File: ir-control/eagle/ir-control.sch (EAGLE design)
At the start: 31 parts, among them J1 MICRO USB, J2 MICRO USB, J3 MICRO USB, Q1 DTA114EET1G (2x10K), Q3 NPN, U2 NUF2042XV6T1G, U3 LPC11U35FHI33/501, U4 MCP1754ST-3302E/CB, X1 KLBR1, Y1 12Mhz

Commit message: Some cleanups.
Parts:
- removed C17: 0.1uF, ir-control:CC0402K
- removed R13: 1K5, ir-control:RR0402
- removed U4: MCP1754ST-3302E/CB, ir-control:LDO
- removed X1: KLBR1, ir-control:KLBR1
- added C9: 0.1uF, ir-control:CC0402K
- added J4: JACKX, ir-control:JACKX
- added R8: 10K, ir-control:RR0402
- added U1: NUF2042XV6T1G, ir-control:USB-ESD
- C1: value 18pF -> 10u; device ir-control:CC0402K -> ir-control:CC0805K
- C2: value 18pF -> 1u; device ir-control:CC0402K -> ir-control:CC0603K
- C3: value 0.1uF -> 1u; device ir-control:CC0402K -> ir-control:CC0603K
- C4: value 0.1uF -> 10u; device ir-control:CC0402K -> ir-control:CC0805K
- C5: value 10u -> 18pF; device ir-control:CC0805K -> ir-control:CC0402K
- C6: value 1u -> 18pF; device ir-control:CC0603K -> ir-control:CC0402K
- C7: value 1u -> 0.1uF; device ir-control:CC0603K -> ir-control:CC0402K
- C8: value 10u -> 0.1uF; device ir-control:CC0805K -> ir-control:CC0402K
- R1: value 1K5 -> 10K
- R3: value 10K -> 1K5
- R5, R7: value 10K -> 330
- R6: value 330 -> 1K5
- U2: value NUF2042XV6T1G -> MCP1754ST-3302E/CB; device ir-control:USB-ESD -> ir-control:LDO
- renumbered D3 to D1, Y1 to Q2
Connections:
- net !ISP_EN: now also C9.2; no longer C17.2
- net !RESET: now also R8.1; no longer R3.1
- net +3V3: now also C7.1, C8.1, C9.1, R8.2; no longer C17.1, C3.1, C4.1, R3.2
- net +5V: now also C1.1, C2.1, J3.VBUS, R4.1, R7.2, U1.VBUS, U2.VIN; no longer C5.1, C6.1, J1.VBUS, R2.1, R6.2, U2.VBUS, U4.VIN
- net AV_SENSE: now also R2.2, U3.TD/AD0/CT32B0_MAT3/PIO0_11; no longer R5.2
- net GND: now also U1.GND; no longer U4.GND
- net IR: now also R6.2; no longer R7.2
- net LED: now also R5.1; no longer R13.1
- net N$1: now also C5.1; no longer C1.1
- net N$12: now also J3.D-, U1.DMI; no longer J1.D-, U2.DMI
- net N$14: now also R5.2; no longer R13.2
- net N$2: now also J1.VBUS, R1.1; no longer J2.VBUS, R4.1
- net N$3: now also C6.1; no longer C2.1
- net N$4: now also R6.1; no longer R7.1
- net N$5: now also R3.2; no longer R1.2
- net N$6: now also J3.D+, R3.1, U1.DPI; no longer J1.D+, R1.1, U2.DPI
- net N$7: now also J2.VBUS, R2.1; no longer J3.VBUS, R5.1
- net TV_SENSE: now also R1.2, U3.SWCLK/SCK0/CT16B0_MAT2/PIO0_10; no longer R4.2
- net USB_DM: now also U1.DMO; no longer U2.DMO
- net USB_DP: now also U1.DPO; no longer U2.DPO
- net VBUS: now also R4.2; no longer R2.2
- net VOUT: now also C3.1, C4.1, U2.VOUT; no longer C7.1, C8.1, U4.VOUT
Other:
- moved on the sheet: C1, C2, C3, C4, C5, C6, C7, C8, J1, J2, J3, R1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

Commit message: More progress with the layout.
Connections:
- removed net VOUT: C3.1, C4.1, U2.VOUT
- net +3V3: now also C3.1, C4.1, U2.VOUT
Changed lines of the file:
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@@
 <attribute name="VALUE" x="345.186" y="262.382" size="1.778" layer="96"/>
 </instance>
-<instance part="+3V35" gate="G$1" x="342.9" y="271.78"/>
+<instance part="+3V35" gate="G$1" x="342.9" y="274.32"/>
 <instance part="S2" gate="G$1" x="383.54" y="83.82" smashed="yes">
 <attribute name="NAME" x="377.952" y="79.248" size="1.778" layer="95"/>
@@
 <pinref part="R8" gate="G$1" pin="2"/>
 <pinref part="+3V35" gate="G$1" pin="+3V3"/>
+<wire x1="342.9" y1="271.78" x2="342.9" y2="269.24" width="0.1524" layer="91"/>
 </segment>
 <segment>
@@
 <wire x1="350.52" y1="109.22" x2="350.52" y2="111.76" width="0.1524" layer="91"/>
 <pinref part="+3V36" gate="G$1" pin="+3V3"/>
+</segment>
+<segment>
+<pinref part="C3" gate="G$1" pin="1"/>
+<wire x1="210.82" y1="119.38" x2="220.98" y2="119.38" width="0.1524" layer="91"/>
+<wire x1="220.98" y1="119.38" x2="226.06" y2="119.38" width="0.1524" layer="91"/>
+<wire x1="210.82" y1="114.3" x2="210.82" y2="119.38" width="0.1524" layer="91"/>
+<pinref part="+3V32" gate="G$1" pin="+3V3"/>
+<wire x1="220.98" y1="114.3" x2="220.98" y2="119.38" width="0.1524" layer="91"/>
+<junction x="220.98" y="119.38"/>
+<pinref part="C4" gate="G$1" pin="1"/>
+<pinref part="U2" gate="G$1" pin="VOUT"/>
+<wire x1="205.74" y1="119.38" x2="210.82" y2="119.38" width="0.1524" layer="91"/>
+<junction x="210.82" y="119.38"/>
 </segment>
 </net>
@@
 </segment>
 </net>
-<net name="VOUT" class="0">
-<segment>
-<pinref part="C3" gate="G$1" pin="1"/>
-<wire x1="210.82" y1="119.38" x2="220.98" y2="119.38" width="0.1524" layer="91"/>
-<wire x1="220.98" y1="119.38" x2="226.06" y2="119.38" width="0.1524" layer="91"/>
-<wire x1="210.82" y1="114.3" x2="210.82" y2="119.38" width="0.1524" layer="91"/>
-<pinref part="+3V32" gate="G$1" pin="+3V3"/>
-<wire x1="220.98" y1="114.3" x2="220.98" y2="119.38" width="0.1524" layer="91"/>
-<junction x="220.98" y="119.38"/>
-<pinref part="C4" gate="G$1" pin="1"/>
-<pinref part="U2" gate="G$1" pin="VOUT"/>
-<wire x1="205.74" y1="119.38" x2="210.82" y2="119.38" width="0.1524" layer="91"/>
-<junction x="210.82" y="119.38"/>
-</segment>
-</net>

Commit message: More layout cleanup. Still incomplete.
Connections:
- net N$2: now also J2.VBUS; no longer J1.VBUS
- net N$7: now also J1.VBUS; no longer J2.VBUS
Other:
- moved on the sheet: J1, J2
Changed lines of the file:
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@@
 <classes>
 <class number="0" name="default" width="0" drill="0">
+<clearance class="0" value="0.205"/>
 </class>
 <class number="1" name="power" width="0.254" drill="0">
 </class>
 <class number="2" name="critical" width="0" drill="0">
+<clearance class="0" value="0.205"/>
+<clearance class="1" value="0.205"/>
+<clearance class="2" value="0.205"/>
 </class>
 </classes>
@@
 <part name="C4" library="ir-control" deviceset="C" device="C0805K" value="10u"/>
 <part name="U2" library="ir-control" deviceset="LDO" device="" value="MCP1754ST-3302E/CB"/>
+<part name="J2" library="ir-control" deviceset="USB-CONN" device="" value="MICRO USB"/>
 <part name="J1" library="ir-control" deviceset="USB-CONN" device="" value="MICRO USB"/>
-<part name="J2" library="ir-control" deviceset="USB-CONN" device="" value="MICRO USB"/>
 <part name="GND1" library="ir-control" deviceset="GND" device=""/>
 <part name="GND2" library="ir-control" deviceset="GND" device=""/>
@@
 <attribute name="VALUE" x="182.88" y="124.46" size="1.778" layer="96"/>
 </instance>
-<instance part="J1" gate="G$1" x="40.64" y="137.16"/>
-<instance part="J2" gate="G$1" x="40.64" y="73.66"/>
+<instance part="J2" gate="G$1" x="40.64" y="137.16"/>
+<instance part="J1" gate="G$1" x="40.64" y="73.66"/>
 <instance part="GND1" gate="1" x="50.8" y="127"/>
 <instance part="GND2" gate="1" x="50.8" y="63.5"/>
@@
 </segment>
 <segment>
-<pinref part="J2" gate="G$1" pin="GND"/>
+<pinref part="J1" gate="G$1" pin="GND"/>
 <pinref part="GND2" gate="1" pin="GND"/>
 <wire x1="48.26" y1="68.58" x2="50.8" y2="68.58" width="0.1524" layer="91"/>
@@
 </segment>
 <segment>
-<pinref part="J1" gate="G$1" pin="GND"/>
+<pinref part="J2" gate="G$1" pin="GND"/>
 <pinref part="GND1" gate="1" pin="GND"/>
 <wire x1="48.26" y1="132.08" x2="50.8" y2="132.08" width="0.1524" layer="91"/>
@@
 <net name="N$2" class="0">
 <segment>
-<pinref part="J1" gate="G$1" pin="VBUS"/>
+<pinref part="J2" gate="G$1" pin="VBUS"/>
 <pinref part="R1" gate="G$1" pin="1"/>
 <wire x1="48.26" y1="152.4" x2="55.88" y2="152.4" width="0.1524" layer="91"/>
@@
 <net name="N$7" class="0">
 <segment>
-<pinref part="J2" gate="G$1" pin="VBUS"/>
+<pinref part="J1" gate="G$1" pin="VBUS"/>
 <pinref part="R2" gate="G$1" pin="1"/>
 <wire x1="48.26" y1="88.9" x2="55.88" y2="88.9" width="0.1524" layer="91"/>

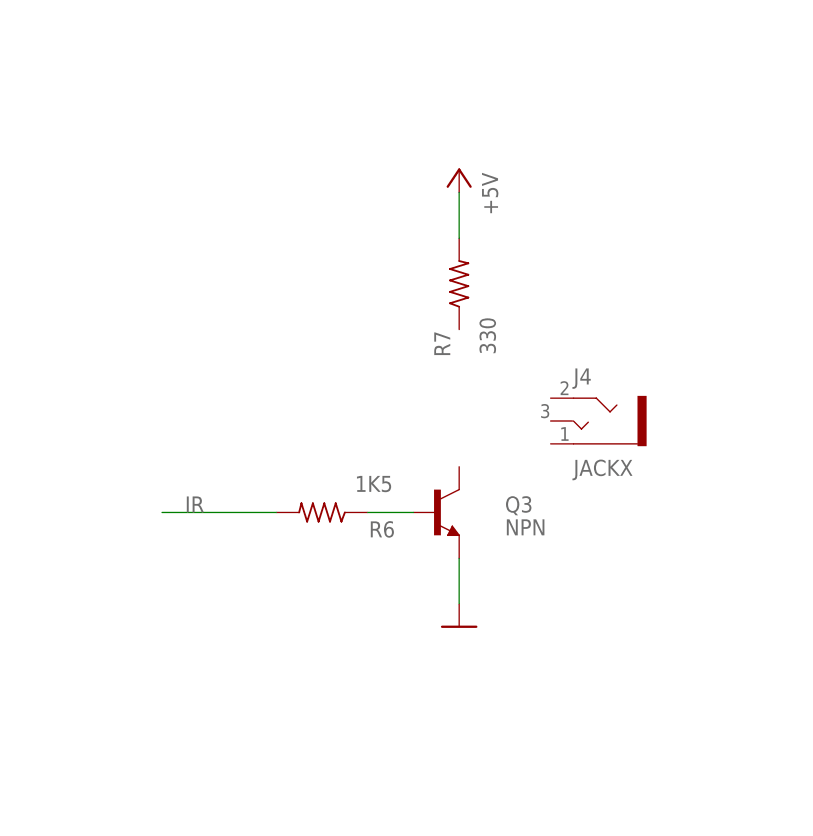
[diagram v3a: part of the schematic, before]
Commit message: Added ir jack.
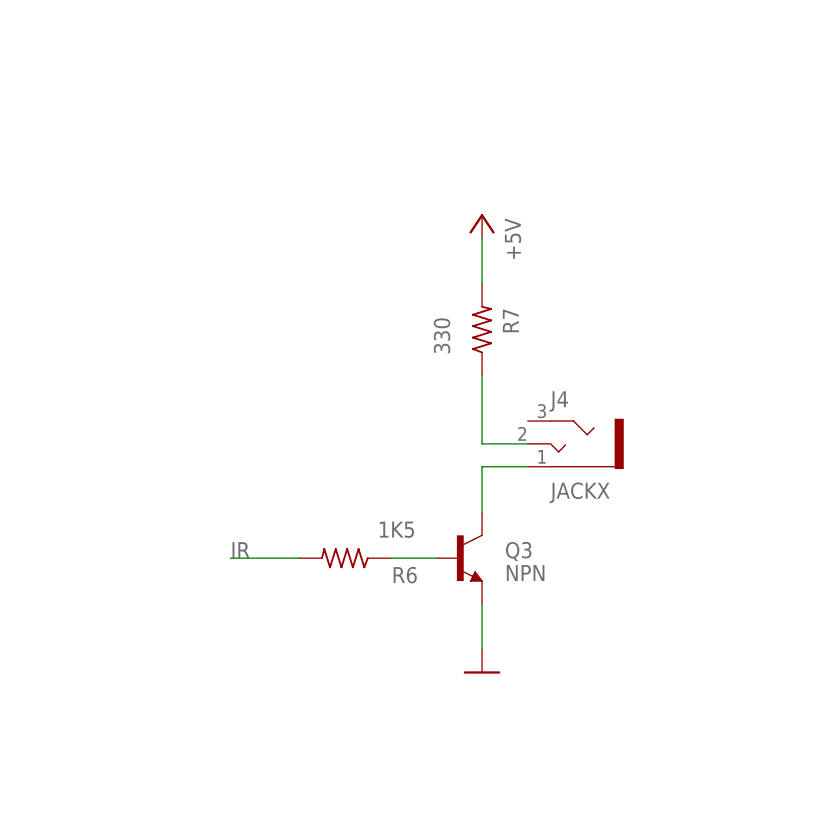
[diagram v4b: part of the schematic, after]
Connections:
- new net N$8: J4.1, Q3.C
- new net N$9: J4.2, R7.1
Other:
- moved on the sheet: J4, Q3, R6, R7
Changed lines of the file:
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@@
 <attribute name="VALUE" x="53.086" y="84.836" size="1.778" layer="96"/>
 </instance>
-<instance part="J4" gate="G$1" x="299.72" y="104.14"/>
-<instance part="+5V3" gate="G$1" x="284.48" y="132.08" rot="MR0"/>
-<instance part="R7" gate="G$1" x="284.48" y="119.38" smashed="yes" rot="R90">
-<attribute name="NAME" x="283.4894" y="111.252" size="1.778" layer="95" rot="R90"/>
-<attribute name="VALUE" x="288.544" y="111.506" size="1.778" layer="96" rot="R90"/>
+<instance part="J4" gate="G$1" x="297.18" y="101.6"/>
+<instance part="+5V3" gate="G$1" x="287.02" y="127" rot="MR0"/>
+<instance part="R7" gate="G$1" x="287.02" y="114.3" smashed="yes" rot="R90">
+<attribute name="NAME" x="291.1094" y="113.792" size="1.778" layer="95" rot="R90"/>
+<attribute name="VALUE" x="283.464" y="111.506" size="1.778" layer="96" rot="R90"/>
 </instance>
-<instance part="GND14" gate="1" x="284.48" y="81.28"/>
-<instance part="Q3" gate="G$1" x="281.94" y="93.98" smashed="yes">
-<attribute name="NAME" x="289.56" y="93.98" size="1.778" layer="95"/>
-<attribute name="VALUE" x="289.56" y="91.44" size="1.778" layer="96"/>
+<instance part="GND14" gate="1" x="287.02" y="76.2"/>
+<instance part="Q3" gate="G$1" x="284.48" y="88.9" smashed="yes">
+<attribute name="NAME" x="289.56" y="88.9" size="1.778" layer="95"/>
+<attribute name="VALUE" x="289.56" y="86.36" size="1.778" layer="96"/>
 </instance>
-<instance part="R6" gate="G$1" x="269.24" y="93.98" smashed="yes" rot="R180">
-<attribute name="NAME" x="277.368" y="92.9894" size="1.778" layer="95" rot="R180"/>
-<attribute name="VALUE" x="277.114" y="98.044" size="1.778" layer="96" rot="R180"/>
+<instance part="R6" gate="G$1" x="271.78" y="88.9" smashed="yes" rot="R180">
+<attribute name="NAME" x="279.908" y="87.9094" size="1.778" layer="95" rot="R180"/>
+<attribute name="VALUE" x="279.654" y="92.964" size="1.778" layer="96" rot="R180"/>
 </instance>
 </instances>
@@
 <pinref part="Q3" gate="G$1" pin="E"/>
 <pinref part="GND14" gate="1" pin="GND"/>
-<wire x1="284.48" y1="83.82" x2="284.48" y2="88.9" width="0.1524" layer="91"/>
+<wire x1="287.02" y1="78.74" x2="287.02" y2="83.82" width="0.1524" layer="91"/>
 </segment>
 </net>
@@
 <segment>
 <pinref part="R7" gate="G$1" pin="2"/>
-<wire x1="284.48" y1="124.46" x2="284.48" y2="129.54" width="0.1524" layer="91"/>
+<wire x1="287.02" y1="119.38" x2="287.02" y2="124.46" width="0.1524" layer="91"/>
 <pinref part="+5V3" gate="G$1" pin="+5V"/>
 </segment>
@@
 <pinref part="R6" gate="G$1" pin="1"/>
 <pinref part="Q3" gate="G$1" pin="B"/>
-<wire x1="274.32" y1="93.98" x2="279.4" y2="93.98" width="0.1524" layer="91"/>
+<wire x1="276.86" y1="88.9" x2="281.94" y2="88.9" width="0.1524" layer="91"/>
 </segment>
 </net>
@@
 <segment>
 <pinref part="R6" gate="G$1" pin="2"/>
-<wire x1="264.16" y1="93.98" x2="251.46" y2="93.98" width="0.1524" layer="91"/>
-<label x="254" y="93.98" size="1.778" layer="95"/>
+<wire x1="266.7" y1="88.9" x2="259.08" y2="88.9" width="0.1524" layer="91"/>
+<label x="259.08" y="88.9" size="1.778" layer="95"/>
 </segment>
 <segment>
@@
 </segment>
 </net>
+<net name="N$8" class="0">
+<segment>
+<pinref part="J4" gate="G$1" pin="1"/>
+<pinref part="Q3" gate="G$1" pin="C"/>
+<wire x1="292.1" y1="99.06" x2="287.02" y2="99.06" width="0.1524" layer="91"/>
+<wire x1="287.02" y1="99.06" x2="287.02" y2="93.98" width="0.1524" layer="91"/>
+</segment>
+</net>
+<net name="N$9" class="0">
+<segment>
+<pinref part="J4" gate="G$1" pin="2"/>
+<pinref part="R7" gate="G$1" pin="1"/>
+<wire x1="292.1" y1="101.6" x2="287.02" y2="101.6" width="0.1524" layer="91"/>
+<wire x1="287.02" y1="101.6" x2="287.02" y2="109.22" width="0.1524" layer="91"/>
+</segment>
+</net>

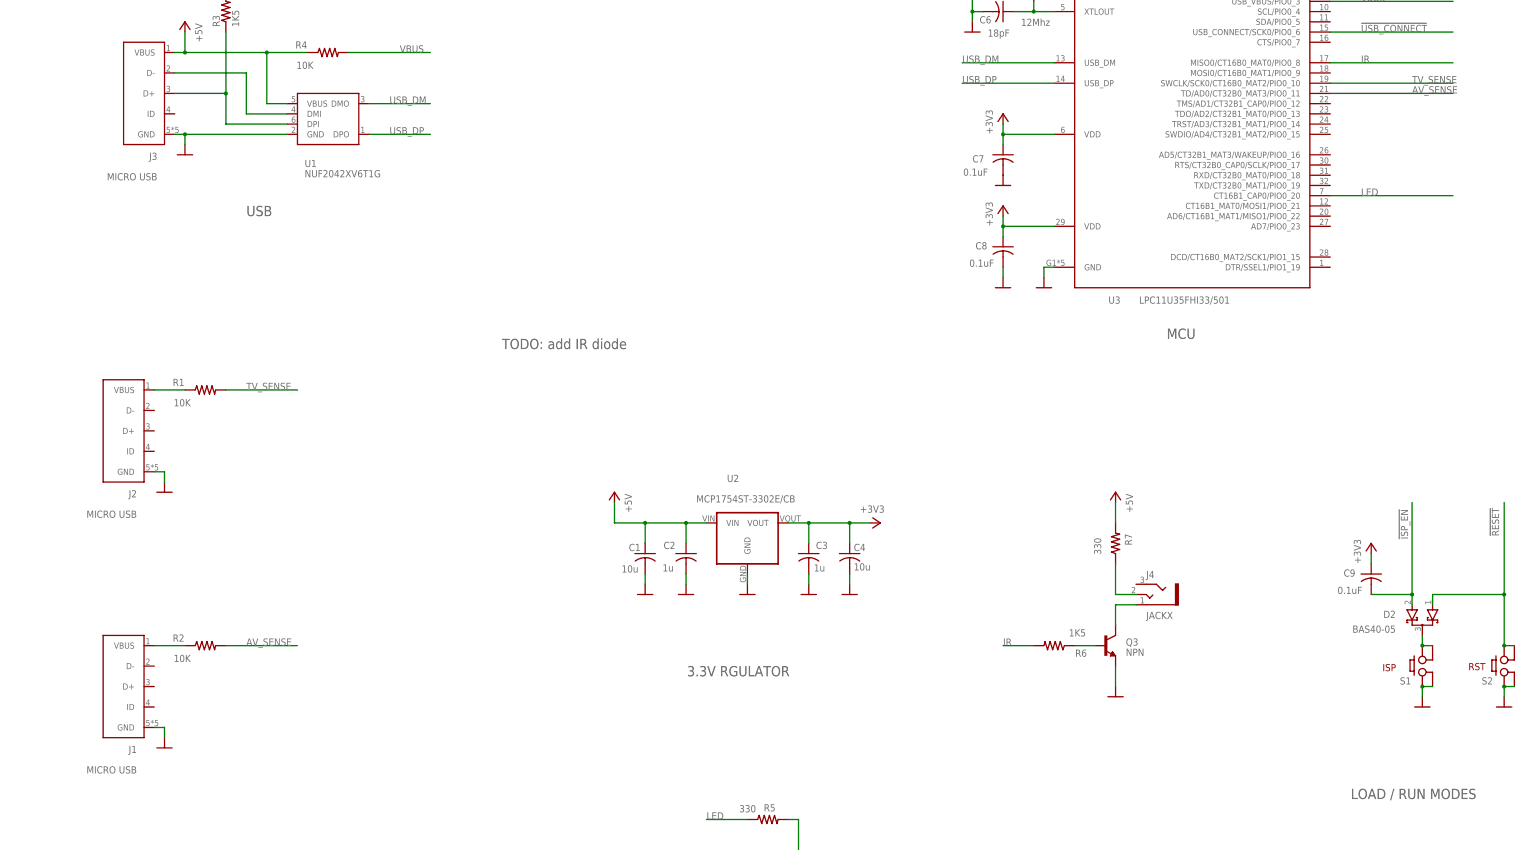
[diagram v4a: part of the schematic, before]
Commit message: Added opto couplers.
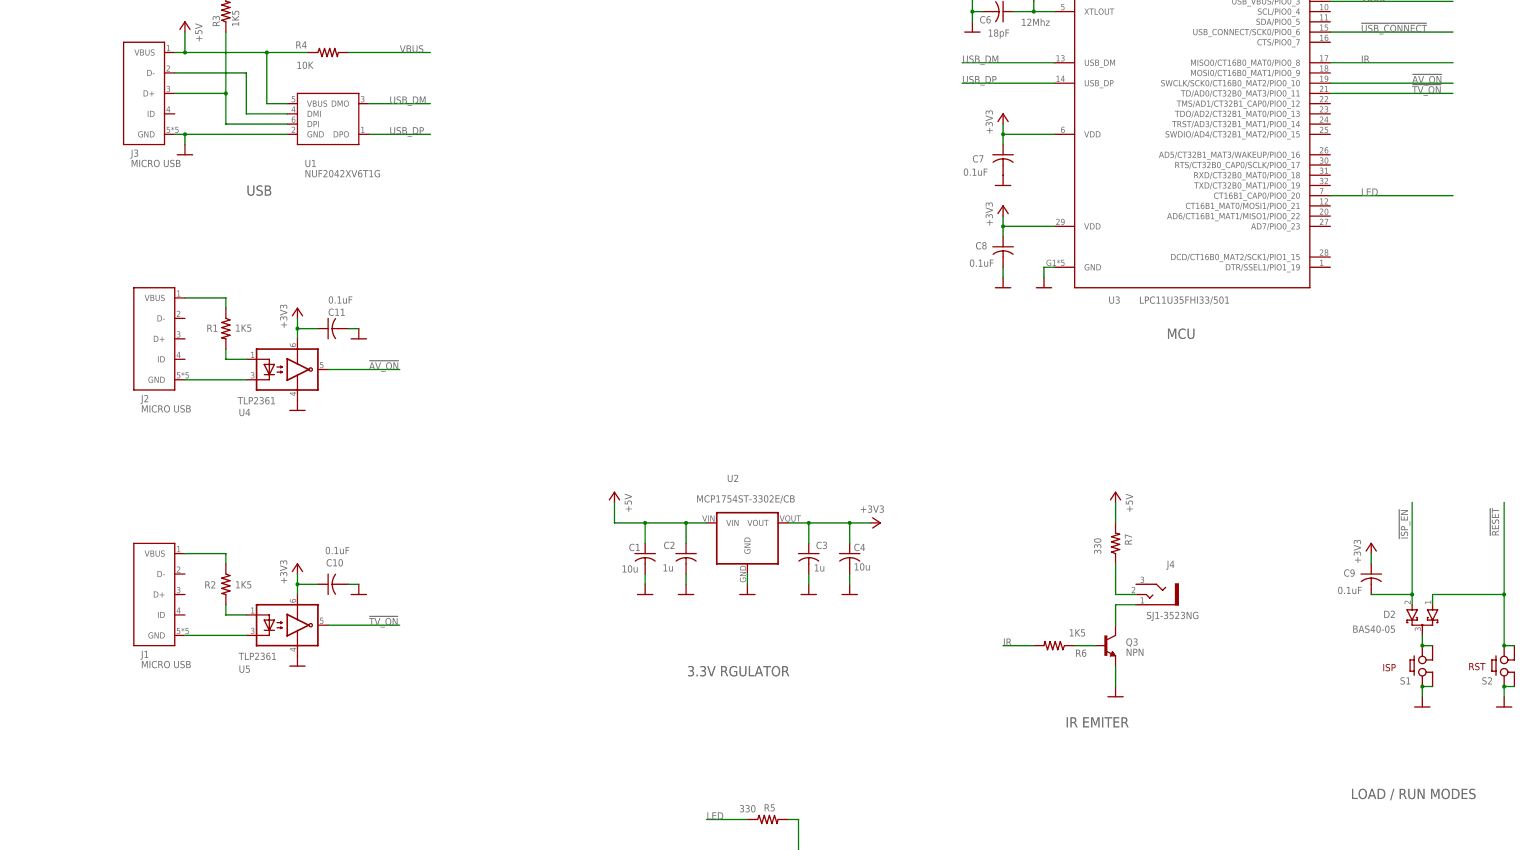
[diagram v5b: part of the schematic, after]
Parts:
- added C10, C11: 0.1uF, ir-control:CC0402K
- added U4, U5: TLP2361, ir-control:OPTO_COUPLER
- J4: value JACKX -> SJ1-3523NG
- R1, R2: value 10K -> 1K5
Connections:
- removed net AV_SENSE: R2.2, U3.TD/AD0/CT32B0_MAT3/PIO0_11
- removed net TV_SENSE: R1.2, U3.SWCLK/SCK0/CT16B0_MAT2/PIO0_10
- new net !AV_ON: U3.SWCLK/SCK0/CT16B0_MAT2/PIO0_10, U4.OUT
- new net !TV_ON: U3.TD/AD0/CT32B0_MAT3/PIO0_11, U5.OUT
- new net N$10: J2.GND, U4.C
- new net N$11: J1.GND, U5.C
- new net N$13: R2.2, U5.A
- new net N$15: R1.2, U4.A
- net +3V3: now also C10.1, C11.1, U4.VCC, U5.VCC
- net GND: now also C10.2, C11.2, U4.GND, U5.GND; no longer J1.GND, J2.GND
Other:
- note added: "IR EMITER"
- note removed: "TODO: add IR diode"
- moved on the sheet: J1, J2, R1, R2

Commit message: Minor tweaks.
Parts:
- Q3: value NPN -> MMBT2222A
- S1: value PUSH-BUTTON -> CKN10502CT-ND
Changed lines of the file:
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@@
 <part name="+5V1" library="ir-control" deviceset="+5V" device=""/>
 <part name="GND15" library="ir-control" deviceset="GND" device=""/>
-<part name="S1" library="ir-control" deviceset="PUSH-BUTTON" device=""/>
+<part name="S1" library="ir-control" deviceset="PUSH-BUTTON" device="" value="CKN10502CT-ND"/>
 <part name="GND6" library="ir-control" deviceset="GND" device=""/>
 <part name="C3" library="ir-control" deviceset="C" device="C0603K" value="1u"/>
@@
 <part name="R7" library="ir-control" deviceset="R" device="R0402" value="330"/>
 <part name="GND14" library="ir-control" deviceset="GND" device=""/>
-<part name="Q3" library="ir-control" deviceset="NPN" device=""/>
+<part name="Q3" library="ir-control" deviceset="NPN" device="" value="MMBT2222A"/>
 <part name="R6" library="ir-control" deviceset="R" device="R0402" value="1K5"/>
 <part name="U5" library="ir-control" deviceset="OPTO_COUPLER" device="" value="TLP2361"/>
